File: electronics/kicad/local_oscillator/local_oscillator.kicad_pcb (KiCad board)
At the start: 2 copper layers, 6 parts, among them U1 CE3520K3

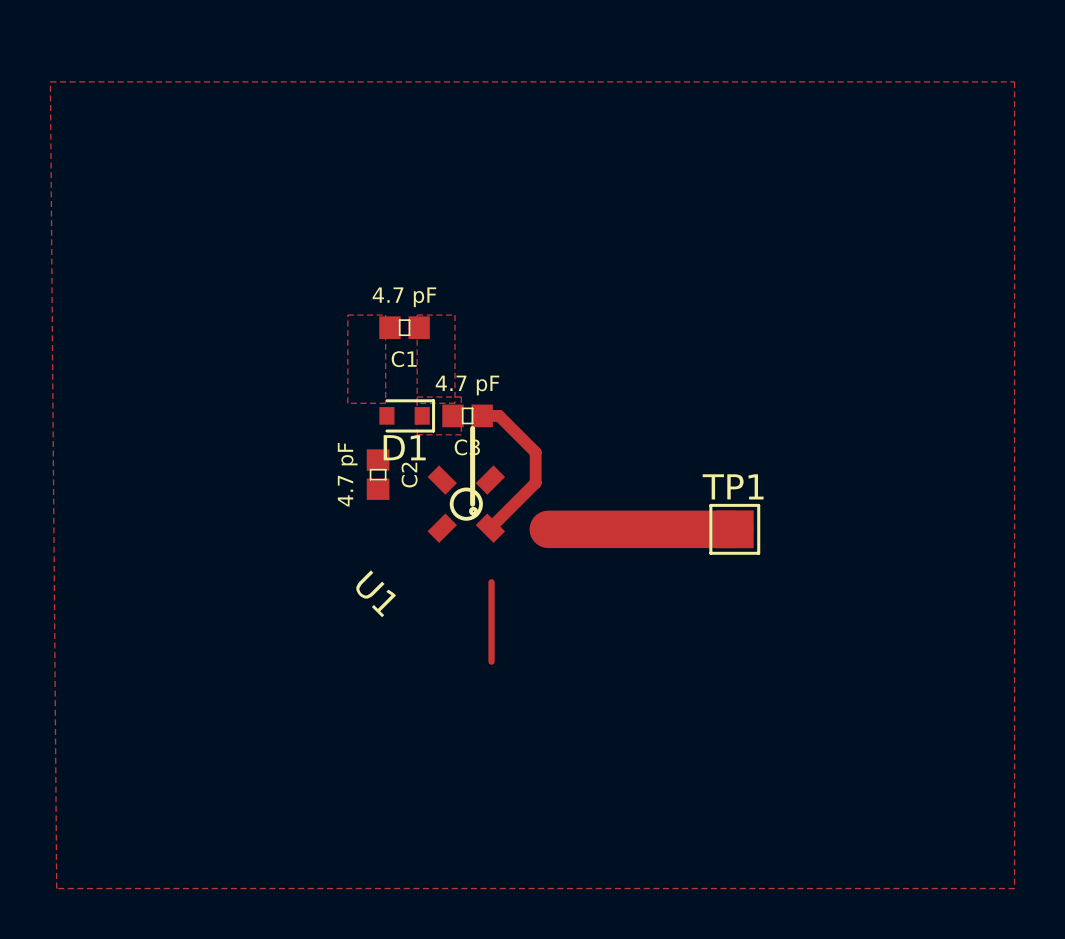
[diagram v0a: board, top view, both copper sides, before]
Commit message: Somewhat altered fb loop
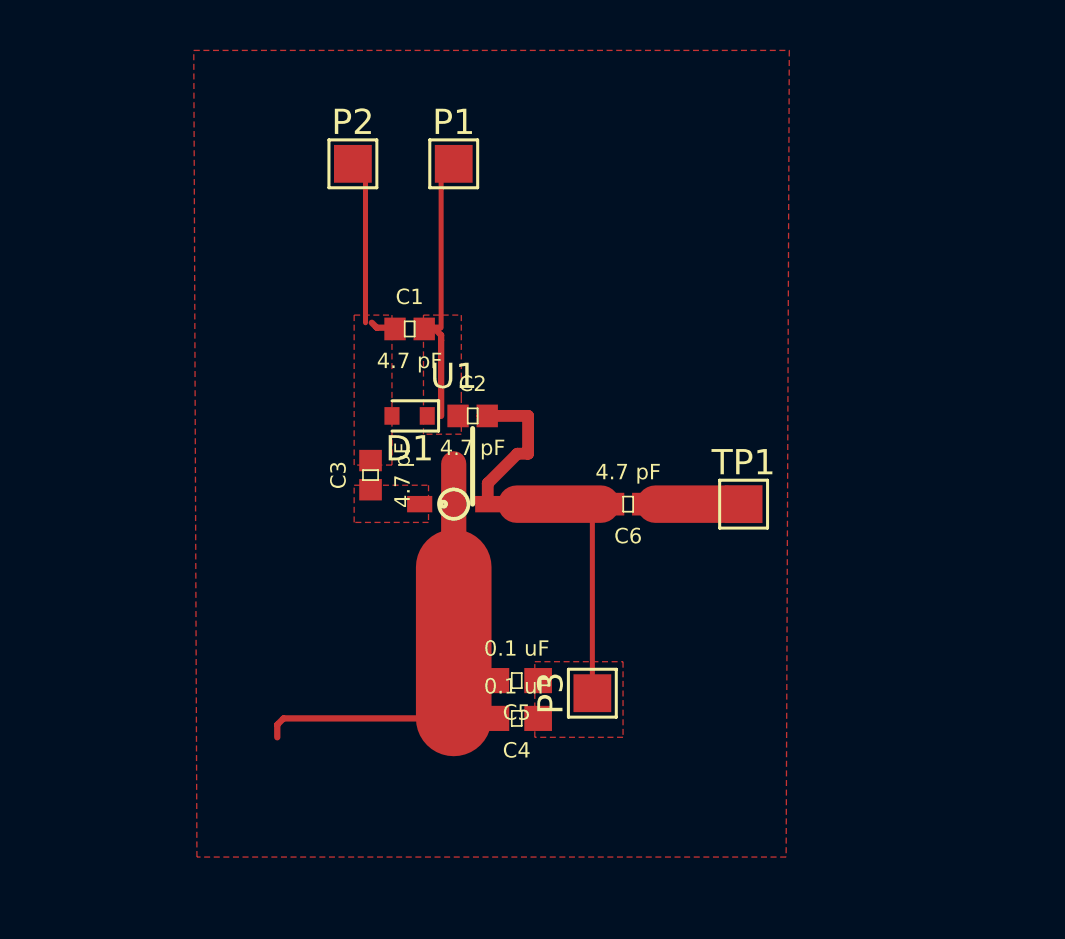
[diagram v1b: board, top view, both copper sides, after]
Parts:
- added C4: 0.1 uF, Capacitors:0603, F.Cu at (63.5, 52.5)
- added C5: 0.1 uF, Capacitors:0603, F.Cu at (63.5, 51.0)
- added C6: 4.7 pF, Capacitors:0402, F.Cu at (67.9, 44.0)
- added P1: TestPoint:TestPoint_Pad_1.5x1.5mm, TestPoint:TestPoint_Pad_1.5x1.5mm, F.Cu at (61.0, 30.5)
- added P2: TestPoint:TestPoint_Pad_1.5x1.5mm, TestPoint:TestPoint_Pad_1.5x1.5mm, F.Cu at (57.0, 30.5)
- added P3: TestPoint:TestPoint_Pad_1.5x1.5mm, TestPoint:TestPoint_Pad_1.5x1.5mm, F.Cu at (66.5, 51.5)
- C2: footprint 0402 -> Capacitors:0402
- D1: value DIODE -> D
- TP1: value TEST-POINT3X4 -> SMA
- moved C3 4.51 mm to (57.7, 42.9), turned to 90 degrees
- moved C2 4.41 mm to (61.8, 40.5), turned to 0 degrees
- moved TP1 1.06 mm to (72.5, 44.0)
- moved U1 0.50 mm to (61.0, 44.0), turned to 180 degrees
- moved C1 0.21 mm to (59.2, 37.0), turned to 0 degrees
- moved D1 0.20 mm to (59.2, 40.5)
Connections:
- net Net-(C3-Pad1) renamed /GATE
- net VCC renamed /VCC
- C1 pad 1: VCO -> /VCO1
- C1 pad 2: Net-(C1-Pad2) -> /VCO2
- C2 pad 1: Net-(C1-Pad2) -> /VCO2
- C3 pad 2: VCO -> /VCO1
- D1 pad 1: VCO -> /VCO2
- D1 pad 2: Net-(C1-Pad2) -> /VCO1
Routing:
- net /VCC: track 0.00 -> 17.1 mm
- net GND: track 3.15 -> 16.3 mm
- net /VCO2: track 0.00 -> 10.3 mm
- net /VCO1: track 0.00 -> 6.76 mm
- net /GATE: track 6.47 -> 0.00 mm
- net (no net): track 7.40 -> 2.75 mm
- added copper zone on F.Cu, net /GATE
- added copper zone on F.Cu, net /VCO1
- added copper zone on F.Cu, net /VCO2
- added copper zone on F.Cu, net VCC
- removed copper zone on F.Cu, net Net-(C1-Pad2)
- removed copper zone on F.Cu, net VCO

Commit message: Series inductor, possible X band downconversion?
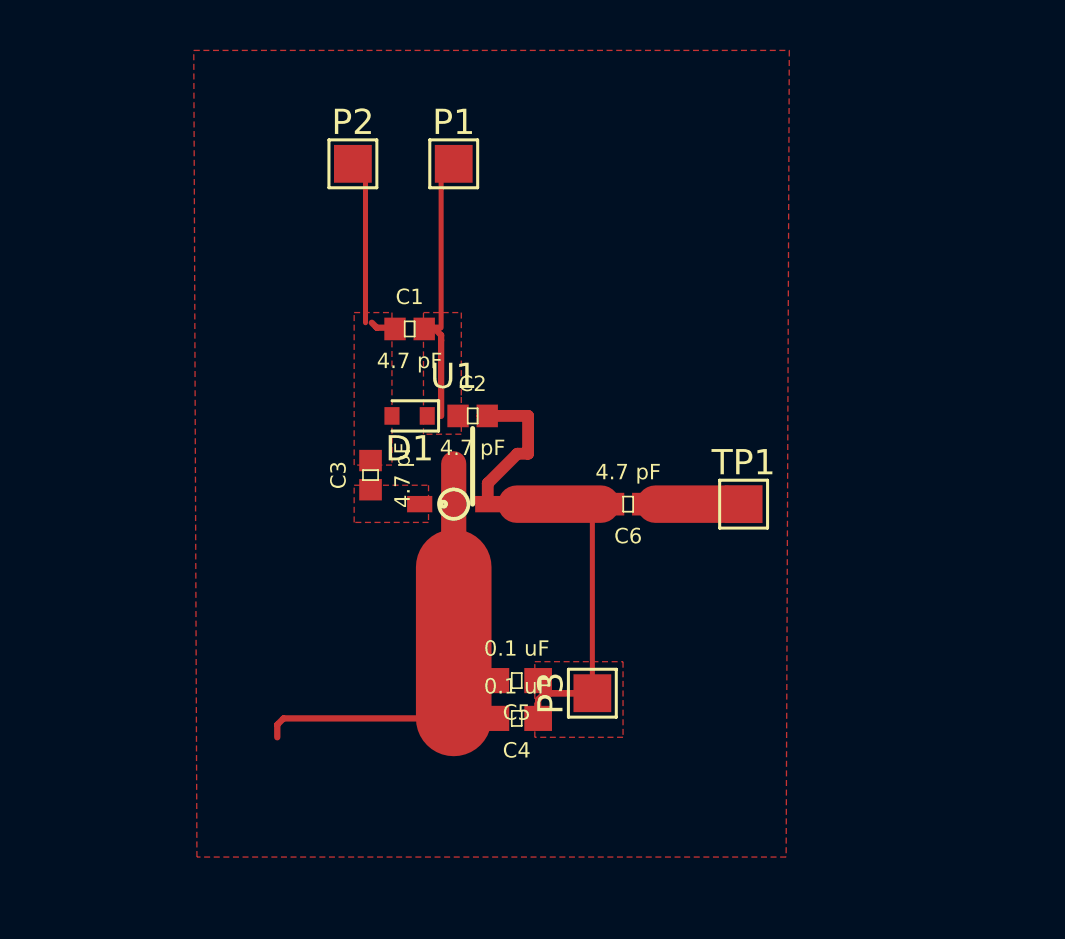
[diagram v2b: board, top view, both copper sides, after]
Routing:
- net /VCC: track 17.1 -> 22.3 mm
- added copper zone on F.Cu, net /VCC
- removed copper zone on F.Cu, net VCC
